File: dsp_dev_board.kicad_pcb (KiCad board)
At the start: 2 copper layers, 100 x 95 mm, 80 parts, among them J1 aux_mcu_power, J10 DX07S016JA1R1500, J11 I2Sext_SD, J12 I2S_SD, J13 SDOUT, J14 ~CSB, J15 I2S2_MCK, J16 WCLK, J17 BCLK, J18 SCLK, J2 audio_in, J3 audio_out, J4 9v_jack, J5 input_jack, J6 output_jack, J7 PD8-15 (digital), J8 PA0-7 (analog), J9 debug, U1 TL072, U2 AMS1117-3.3, U3 STM32F407VETx, U4 WM8731SEDS, Y1 8Mhz

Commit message: Progress
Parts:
- moved J13 115.3 mm to (211.4, 83.7)
- moved J15 105.5 mm to (205.7, 83.1)
- moved J16 96.5 mm to (200.3, 83.4)
- moved J17 86.2 mm to (194.6, 83.7)
- moved J18 85.7 mm to (178.5, 83.9)
- moved J14 75.8 mm to (183.3, 83.8)
- moved J12 69.9 mm to (174.2, 83.8)
- moved S1 68.8 mm to (148.7, 51.5)
- moved J9 66.0 mm to (195.2, 53.8)
- moved J11 65.8 mm to (188.5, 83.9)
- moved J1 63.9 mm to (166.1, 83.9)
- moved J7 55.3 mm to (211.2, 54.4), turned to 0 degrees
- moved D4 52.0 mm to (188.0, 46.7), turned to 270 degrees
- moved S2 49.0 mm to (141.6, 59.5), turned to 180 degrees
- moved D3 47.3 mm to (191.6, 46.7), turned to 90 degrees
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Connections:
- U1 pad 1: Net-(C4-Pad2) -> Net-(C5-Pad2)
- U1 pad 2: Net-(R5-Pad1) -> Net-(R6-Pad1)
- U1 pad 6: Net-(R6-Pad1) -> Net-(R5-Pad1)
- U1 pad 7: Net-(C5-Pad2) -> Net-(C4-Pad2)
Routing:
- net Net-(J7-Pad8): track 0.00 -> 61.0 mm, vias 0 -> 1
- net Net-(J7-Pad7): track 0.00 -> 59.7 mm, vias 0 -> 1
- net Net-(J7-Pad6): track 0.00 -> 58.9 mm, vias 0 -> 1
- net Net-(J7-Pad5): track 0.00 -> 58.2 mm, vias 0 -> 1
- net Net-(J7-Pad4): track 0.00 -> 57.4 mm, vias 0 -> 1
- net Net-(J7-Pad3): track 0.00 -> 56.6 mm, vias 0 -> 1
- net Net-(J7-Pad2): track 0.00 -> 56.2 mm, vias 0 -> 1
- net Net-(J7-Pad1): track 0.00 -> 54.8 mm, vias 0 -> 1
- net Net-(J8-Pad8): track 0.00 -> 45.0 mm, vias 0 -> 1
- net Net-(J8-Pad5): track 0.00 -> 44.2 mm, vias 0 -> 1
- net Net-(J8-Pad7): track 0.00 -> 44.0 mm, vias 0 -> 1
- net Net-(J8-Pad6): track 0.00 -> 43.9 mm, vias 0 -> 1
- net Net-(J8-Pad4): track 0.00 -> 43.0 mm, vias 0 -> 1
- net Net-(J8-Pad1): track 0.00 -> 41.8 mm, vias 0 -> 1
- net Net-(J8-Pad3): track 0.10 -> 40.2 mm, vias 0 -> 1
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- added copper zone on B.Cu, net 9V
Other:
- board text added: "Analog"
- board text added: "Boot"
- board text added: "PA0"
- board text added: "PA1"
- board text added: "PA2"
- board text added: "PA3"
- board text added: "PA4"
- board text added: "PA5"
- board text added: "PA6"
- board text added: "PA7"
- board text added: "Reset"

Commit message: USB to go
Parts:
- moved J9 63.6 mm to (131.7, 50.1)
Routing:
- net /MCU/OTG_FS_DM: track 0.00 -> 36.6 mm, vias 0 -> 2
- net VBUS: track 11.7 -> 46.6 mm, vias 0 -> 2
- net /MCU/OTG_FS_DP: track 0.00 -> 33.2 mm, vias 0 -> 2
- net 3.3V: track 111.1 -> 129.4 mm, vias 13 -> 17
- net GND: track 24.7 -> 35.5 mm
- net /MCU/NRST: track 20.0 -> 27.4 mm
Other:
- board size 100 x 95 mm -> 100 x 71.3 mm

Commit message: Lots of cleanup
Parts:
- moved J9 45.8 mm to (170.0, 75.3), turned to 270 degrees
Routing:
- net /MCU/SWCLK: track 0.00 -> 32.9 mm, vias 0 -> 3
- net /MCU/SWDIO: track 0.00 -> 27.8 mm, vias 0 -> 3
- net /MCU/TRACESWO: track 0.00 -> 27.4 mm, vias 0 -> 1
- net /audio_out: track 0.00 -> 25.5 mm, vias 0 -> 3
- net /audio_in: track 28.6 -> 49.2 mm, vias 2 -> 3
- net /MCU/NRST: track 27.4 -> 38.9 mm, vias 0 -> 1
- net VBUS: track 46.6 -> 54.4 mm, vias 2 -> 4
- net Net-(C4-Pad2): track 3.82 -> 10.7 mm, vias 0 -> 2
- net 3.3V: track 129.4 -> 124.0 mm

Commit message: Basically done?
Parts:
- removed J12: I2S_SD, Connector_PinHeader_2.54mm:PinHeader_1x02_P2.54mm_Vertical
- removed J13: SDOUT, Connector_PinHeader_2.54mm:PinHeader_1x02_P2.54mm_Vertical
- removed J14: ~CSB, Connector_PinHeader_2.54mm:PinHeader_1x02_P2.54mm_Vertical
- removed J15: I2S2_MCK, Connector_PinHeader_2.54mm:PinHeader_1x02_P2.54mm_Vertical
- removed J16: WCLK, Connector_PinHeader_2.54mm:PinHeader_1x02_P2.54mm_Vertical
- removed J17: BCLK, Connector_PinHeader_2.54mm:PinHeader_1x02_P2.54mm_Vertical
- removed J18: SCLK, Connector_PinHeader_2.54mm:PinHeader_1x02_P2.54mm_Vertical
- J11: value I2Sext_SD -> Conn_02x08_Odd_Even; footprint Connector_PinHeader_2.54mm:PinHeader_1x02_P2.54mm_Vertical -> Connector_PinHeader_2.54mm:PinHeader_2x08_P2.54mm_Vertical
- moved J1 53.2 mm to (124.9, 50.2), turned to 90 degrees
- moved J11 11.1 mm to (193.1, 73.8), turned to 270 degrees
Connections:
- J11 pad 1: /Codec/ADC -> /Codec/~CSB
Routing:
- net /audio_out: track 25.5 -> 70.1 mm, vias 3 -> 4
- net /Codec/~CSB: track 23.7 -> 38.2 mm, vias 1 -> 2
- net /Codec/SDIN: track 24.6 -> 37.5 mm, vias 1 -> 2
- net /Codec/WCLK: track 9.59 -> 21.8 mm
- net /Codec/BCLK: track 6.06 -> 17.9 mm, vias 1 -> 2
- net /Codec/ADC: track 5.84 -> 17.6 mm
- net /Codec/DAC: track 6.61 -> 18.0 mm
- net /Codec/SCLK: track 29.8 -> 39.6 mm, vias 1 -> 2
- net /MCU/I2S2_MCK: track 19.1 -> 28.7 mm, vias 1 -> 2
- net GND: track 35.5 -> 38.4 mm
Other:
- board text added: "DSP dev board v1 by Eric Wood and Matt Mullins"
- board text added: "aux power"

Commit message: it's done
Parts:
- added G***: LOGO, frankie:frankie, F.Cu at (131.2, 66.2)
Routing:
- net 3.3V: track 124.0 -> 130.6 mm, vias 17 -> 18
- net GND: track 38.4 -> 40.2 mm
- net /Codec/DAC: track 18.0 -> 19.3 mm
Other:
- board size 100 x 71.3 mm -> 100 x 60.3 mm
- board text added: "+3.3V"
- board text added: "BCLK"
- board text added: "DSP dev board v1 by Eric Wood"
- board text added: "Debug"
- board text added: "Digital"
- board text added: "GND"
- board text added: "I2S2_MCK"
- board text added: "I2S_SD"
- board text added: "I2Sext_SD"
- board text added: "PB4"
- board text added: "PB5"
- board text added: "PB6"
- board text added: "PB7"
- board text added: "PD10"
- board text added: "PD11"
- board text added: "PD12"
- board text added: "PD13"
- board text added: "PD14"
- board text added: "PD15"
- board text added: "PD8"
- board text added: "PD9"
- board text added: "SCLK"
- board text added: "SDOUT"
- board text added: "WCLK"
- board text added: "audio in"
- board text added: "gnd"
- board text added: "in"
- board text added: "input"
- board text added: "out"
- board text added: "output"
- board text added: "use this to play Frankie something nice"
- board text added: "~CSB"
- board text removed: "DSP dev board v1 by Eric Wood and Matt Mullins"
- board text removed: "aux power"

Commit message: 4 layer progress
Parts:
- removed G***: LOGO, frankie:frankie
- J10: footprint USB_C:JAE_DX07S016JA1R1500 -> DX07S016JA1R1500:JAE_DX07S016JA1R1500
- U4: moved to F.Cu
- moved C20 56.3 mm to (137.0, 95.3)
- moved C19 56.3 mm to (137.0, 93.7)
- moved J9 54.2 mm to (122.6, 101.7), turned to 90 degrees
- moved C18 53.6 mm to (123.5, 96.1)
- moved U2 50.1 mm to (118.8, 61.1), turned to 180 degrees
- moved D5 49.8 mm to (112.0, 69.5), turned to 0 degrees
- moved J2 49.4 mm to (171.5, 70.0)
- moved C1 48.7 mm to (124.8, 62.0), turned to 270 degrees
- moved C11 48.6 mm to (118.9, 82.0), turned to 90 degrees
- moved D6 48.3 mm to (112.0, 71.1), turned to 0 degrees
- moved D1 48.2 mm to (129.8, 63.0), turned to 0 degrees
- moved C17 48.0 mm to (116.6, 92.8)
- moved D7 47.0 mm to (112.0, 72.7), turned to 0 degrees
- moved C16 46.2 mm to (116.6, 89.7), turned to 90 degrees
- moved D8 45.9 mm to (112.0, 74.3), turned to 0 degrees
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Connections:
- R10 pad 1: /MCU/NRST -> 3.3V
- R10 pad 2: GND -> /MCU/NRST
- S2 pad C: 3.3V -> GND
- S2 pad D: 3.3V -> GND
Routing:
- net Net-(J7-Pad8): track 61.0 -> 0.00 mm, vias 1 -> 0
- net Net-(J7-Pad7): track 59.7 -> 0.00 mm, vias 1 -> 0
- net Net-(J7-Pad6): track 58.9 -> 0.00 mm, vias 1 -> 0
- net Net-(J7-Pad5): track 58.2 -> 0.00 mm, vias 1 -> 0
- net Net-(J7-Pad4): track 57.4 -> 0.00 mm, vias 1 -> 0
- net Net-(J7-Pad3): track 56.6 -> 0.00 mm, vias 1 -> 0
- net Net-(J7-Pad2): track 56.2 -> 0.00 mm, vias 1 -> 0
- net Net-(J7-Pad1): track 54.8 -> 0.00 mm, vias 1 -> 0
- net GND: track 40.2 -> 86.2 mm, vias 3 -> 17
- net 3.3V: track 130.6 -> 84.9 mm, vias 18 -> 4
- net Net-(J8-Pad8): track 45.0 -> 0.00 mm, vias 1 -> 0
- net Net-(J8-Pad5): track 44.2 -> 0.00 mm, vias 1 -> 0
- net Net-(J8-Pad7): track 44.0 -> 0.00 mm, vias 1 -> 0
- net Net-(J8-Pad6): track 43.9 -> 0.00 mm, vias 1 -> 0
- net Net-(J8-Pad4): track 43.0 -> 0.00 mm, vias 1 -> 0
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- added copper zone on F.Cu, net 3.3V
- added copper zone on In1.Cu, net GND
- added copper zone on In2.Cu, net GND
- removed copper zone on B.Cu, net 9V
- removed copper zone on F.Cu, net GND
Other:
- board size 100 x 60.3 mm -> 100 x 100 mm
- copper layers 2 -> 4
- board text removed: "+3.3V"
- board text removed: "Analog"
- board text removed: "BCLK"
- board text removed: "Boot"
- board text removed: "DSP dev board v1 by Eric Wood"
- board text removed: "Debug"
- board text removed: "Digital"
- board text removed: "GND"
- board text removed: "I2S2_MCK"
- board text removed: "I2S_SD"
- board text removed: "I2Sext_SD"
- board text removed: "PA0"
- board text removed: "PA1"
- board text removed: "PA2"
- board text removed: "PA3"
- board text removed: "PA4"
- board text removed: "PA5"
- board text removed: "PA6"
- board text removed: "PA7"
- board text removed: "PB4"
- board text removed: "PB5"
- board text removed: "PB6"
- board text removed: "PB7"
- board text removed: "PD10"
- board text removed: "PD11"
- board text removed: "PD12"
- board text removed: "PD13"
- board text removed: "PD14"
- board text removed: "PD15"
- board text removed: "PD8"
- board text removed: "PD9"
- board text removed: "Reset"
- board text removed: "SCLK"
- board text removed: "SDOUT"
- board text removed: "WCLK"
- board text removed: "audio in"
- board text removed: "gnd"
- board text removed: "in"
- board text removed: "input"
- board text removed: "out"
- board text removed: "output"
- board text removed: "use this to play Frankie something nice"
- board text removed: "~CSB"

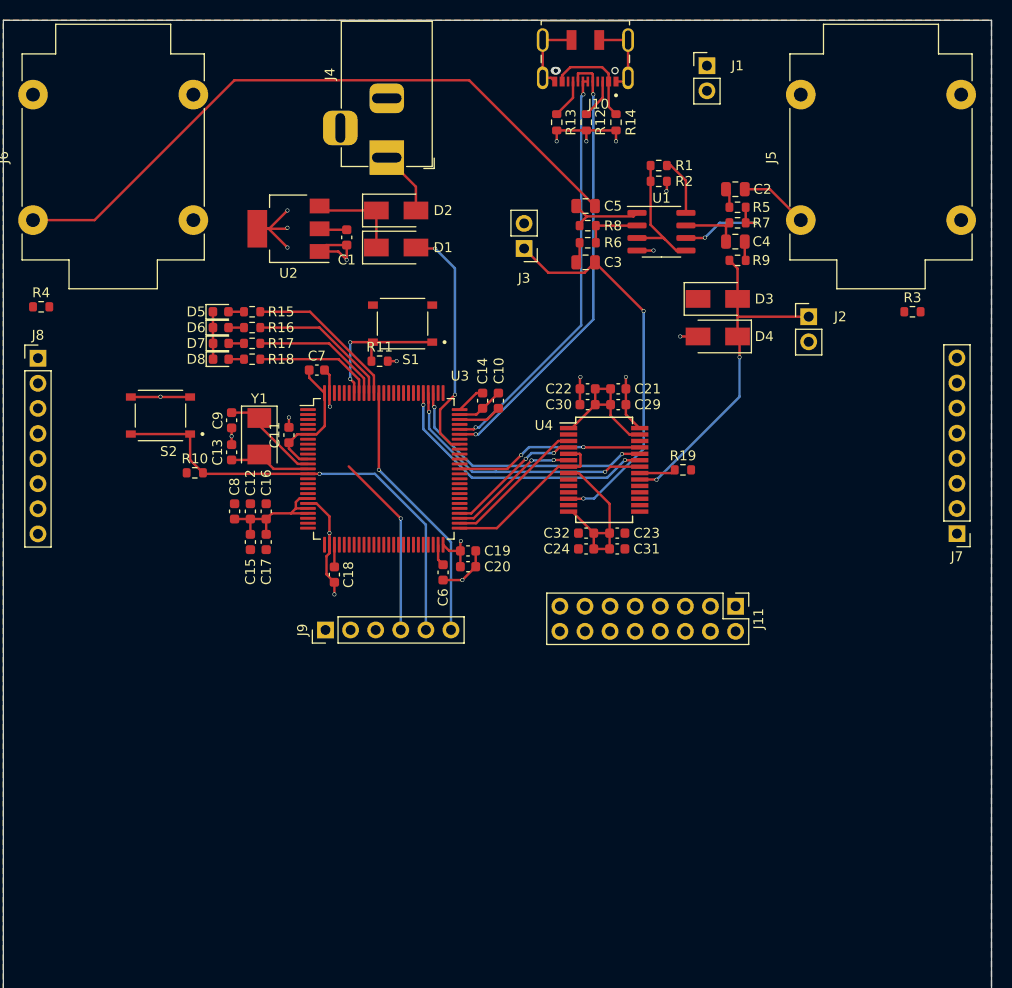
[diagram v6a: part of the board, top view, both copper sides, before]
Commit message: PCB: most major layout with both codec footprints
Surprisingly, I don't hate the really long I2S bus-like formation
between both footprints, though it does break up both the front and back
layers in the same orientation.
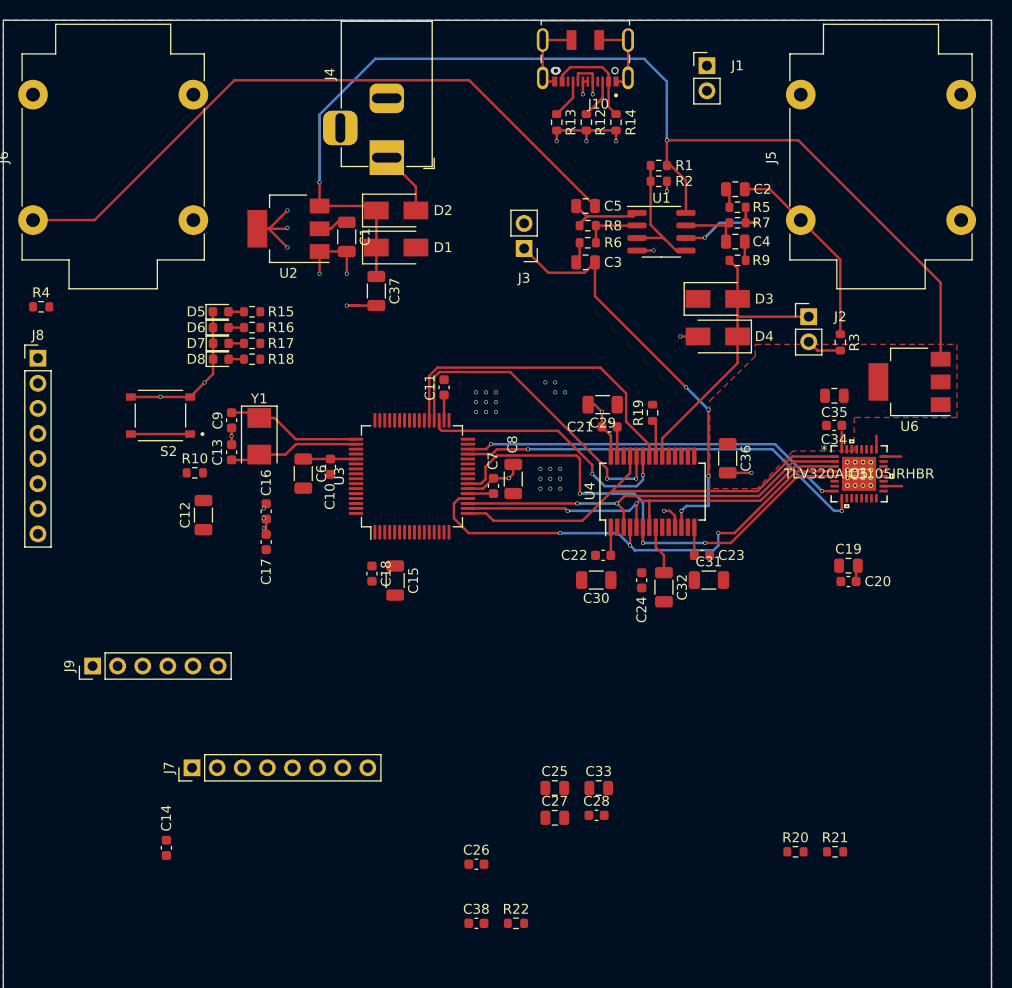
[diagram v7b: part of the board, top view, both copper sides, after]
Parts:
- removed J11: Conn_02x08_Odd_Even, Connector_PinHeader_2.54mm:PinHeader_2x08_P2.54mm_Vertical
- removed R11: 10k, Resistor_SMD:R_0603_1608Metric
- removed S1: TS-1187A-B-A-B, TactileSwitch:SW_TS-1187A-B-A-B
- added C25: 1u, Capacitor_SMD:C_0805_2012Metric, F.Cu at (145.8, 117.7)
- added C26: 100n, Capacitor_SMD:C_0603_1608Metric, F.Cu at (137.9, 125.4)
- added C27: 1u, Capacitor_SMD:C_0805_2012Metric, F.Cu at (145.8, 120.7)
- added C28: 100n, Capacitor_SMD:C_0603_1608Metric, F.Cu at (150.0, 120.5)
- added C33: 1u, Capacitor_SMD:C_0805_2012Metric, F.Cu at (150.2, 117.7)
- added C34: 100n, Capacitor_SMD:C_0603_1608Metric, F.Cu at (174.1, 81.0)
- added C35: 1u, Capacitor_SMD:C_0805_2012Metric, F.Cu at (174.1, 78.0)
- added C36: 10u, Capacitor_SMD:C_1206_3216Metric, F.Cu at (163.3, 84.3)
- added C37: 10u, Capacitor_SMD:C_1206_3216Metric, F.Cu at (127.8, 67.4)
- added C38: 100n, Capacitor_SMD:C_0603_1608Metric, F.Cu at (137.9, 131.4)
- added R20: 10k, Resistor_SMD:R_0603_1608Metric, F.Cu at (170.2, 124.2)
- added R21: 10k, Resistor_SMD:R_0603_1608Metric, F.Cu at (174.2, 124.2)
- added R22: 330, Resistor_SMD:R_0603_1608Metric, F.Cu at (141.9, 131.4)
- added U5: TLV320AIC3105IRHBR, TLV320AIC3105:TLV320AIC3105IRHBR, F.Cu at (176.6, 85.9)
- added U6: AMS1117-1.8, Package_TO_SOT_SMD:SOT-223-3_TabPin2, F.Cu at (181.7, 76.6)
- C1: value 0.1u -> 10u; footprint Capacitor_SMD:C_0603_1608Metric -> Capacitor_SMD:C_1206_3216Metric
- C10: value 2.2u -> 100n
- C12: value 100n -> 10u; footprint Capacitor_SMD:C_0603_1608Metric -> Capacitor_SMD:C_1206_3216Metric
- C15, C8: value 1u -> 10u; footprint Capacitor_SMD:C_0603_1608Metric -> Capacitor_SMD:C_1206_3216Metric
- C19: value 100n -> 1u; footprint Capacitor_SMD:C_0603_1608Metric -> Capacitor_SMD:C_0805_2012Metric
- C20: value 4.7u -> 100n
- C21, C22, C23, C24: value 0.1u -> 100n
- C29, C30, C31, C32: footprint Capacitor_SMD:C_0603_1608Metric -> Capacitor_SMD:C_1206_3216Metric
- C6: value 2.2u -> 10u; footprint Capacitor_SMD:C_0603_1608Metric -> Capacitor_SMD:C_1206_3216Metric
- J10: footprint DX07S016JA1R1500:JAE_DX07S016JA1R1500 -> USB_C:JAE_DX07S016JA1R1500
- J7: value PD8-15 (digital) -> digital
- J8: value PA0-7 (analog) -> analog
- U3: value STM32F407VETx -> ATSAME51J18A-A; footprint Package_QFP:LQFP-100_14x14mm_P0.5mm -> Package_QFP:TQFP-64_10x10mm_P0.5mm
- moved J7 80.9 mm to (109.1, 115.7), turned to 90 degrees
- moved C14 55.4 mm to (106.5, 123.8)
- moved C19 38.5 mm to (175.5, 95.2)
- moved C20 38.5 mm to (175.5, 96.8)
- moved C8 28.4 mm to (141.6, 86.4)
- moved J9 23.9 mm to (99.0, 105.3)
- moved C7 21.4 mm to (139.6, 87.1), turned to 90 degrees
- moved C10 18.3 mm to (123.1, 85.2), turned to 270 degrees
- moved C30 17.8 mm to (150.0, 96.7)
- moved C6 17.3 mm to (120.3, 85.9)
- moved C22 16.9 mm to (150.7, 94.2)
- moved C11 16.4 mm to (134.6, 77.2)
- moved C15 15.2 mm to (129.7, 96.7)
- moved C31 9.80 mm to (161.4, 96.7)
- moved C32 9.59 mm to (156.8, 97.4), turned to 270 degrees
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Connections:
- C10 pad 1: /MCU/VCAP_2 -> Net-(C10-Pad1)
- C17 pad 2: GND -> Net-(C17-Pad2)
- C19 pad 2: GND -> Net-(C17-Pad2)
- C20 pad 2: GND -> Net-(C17-Pad2)
- C6 pad 1: /MCU/VCAP_1 -> Net-(C10-Pad1)
- J7 pad 1: Net-(J7-Pad1) -> /MCU/PB00
- J7 pad 2: Net-(J7-Pad2) -> /MCU/PB01
- J7 pad 3: Net-(J7-Pad3) -> /MCU/PB02
- J7 pad 4: Net-(J7-Pad4) -> /MCU/PB03
- J7 pad 5: Net-(J7-Pad5) -> /MCU/PB04
- J7 pad 6: Net-(J7-Pad6) -> /MCU/PB05
- J7 pad 7: Net-(J7-Pad7) -> /MCU/PB06
- J7 pad 8: Net-(J7-Pad8) -> /MCU/PB07
- J8 pad 1: Net-(J8-Pad1) -> /MCU/PB08
- J8 pad 2: Net-(J8-Pad2) -> /MCU/PB09
- J8 pad 3: Net-(J8-Pad3) -> /MCU/PA02
- J8 pad 4: Net-(J8-Pad4) -> /MCU/PA03
- J8 pad 5: Net-(J8-Pad5) -> /MCU/PA04
- J8 pad 6: Net-(J8-Pad6) -> /MCU/PA05
- J8 pad 7: Net-(J8-Pad7) -> /MCU/PA06
- J8 pad 8: Net-(J8-Pad8) -> /MCU/PA07
- R10 pad 2: /MCU/NRST -> Net-(C38-Pad1)
- U3 pad 10: GND -> /MCU/PB07
- U3 pad 11: 3.3V -> /MCU/PB08
- U3 pad 12: /MCU/osc_in -> /MCU/PB09
- U3 pad 13: /MCU/osc_out -> /MCU/PA04
- U3 pad 14: /MCU/NRST -> /MCU/PA05
- U3 pad 15: Net-(U3-Pad15) -> /MCU/PA06
- U3 pad 16: Net-(U3-Pad16) -> /MCU/PA07
- U3 pad 17: Net-(U3-Pad17) -> /MCU/I2S2_MCK
- U3 pad 18: Net-(U3-Pad18) -> /Codec/WCLK
- U3 pad 19: 3.3V -> /Codec/BCLK
- U3 pad 20: GND -> /Codec/DAC
- U3 pad 22: 3.3V -> GND
- U3 pad 23: Net-(J8-Pad1) -> /Codec/ADC
- U3 pad 24: Net-(J8-Pad2) -> Net-(U3-Pad24)
- U3 pad 25: Net-(J8-Pad3) -> /MCU/led1
- U3 pad 26: Net-(J8-Pad4) -> /MCU/led2
- U3 pad 27: GND -> /MCU/led3
- U3 pad 28: 3.3V -> /MCU/led4
- U3 pad 29: Net-(J8-Pad5) -> /MCU/SDA
- U3 pad 3: Net-(U3-Pad3) -> /MCU/PA02
- U3 pad 30: Net-(J8-Pad6) -> /MCU/SCL
- U3 pad 31: Net-(J8-Pad7) -> /MCU/~CODEC_RST
- U3 pad 32: Net-(J8-Pad8) -> /MCU/BOOT0
- U3 pad 33: Net-(U3-Pad33) -> GND
- U3 pad 34: Net-(U3-Pad34) -> 3.3V
- U3 pad 35: Net-(U3-Pad35) -> /Codec/SDIN
- U3 pad 36: Net-(U3-Pad36) -> /Codec/SCLK
- U3 pad 37: Net-(U3-Pad37) -> /Codec/~CSB
- U3 pad 4: Net-(U3-Pad4) -> /MCU/PA03
- U3 pad 45: Net-(U3-Pad45) -> /MCU/OTG_FS_DM
- U3 pad 46: Net-(U3-Pad46) -> /MCU/OTG_FS_DP
- U3 pad 47: Net-(U3-Pad47) -> GND
- U3 pad 48: Net-(U3-Pad48) -> 3.3V
- U3 pad 49: /MCU/VCAP_1 -> /MCU/osc_in
- U3 pad 5: Net-(U3-Pad5) -> /MCU/PB04
- U3 pad 50: 3.3V -> /MCU/osc_out
- U3 pad 51: /Codec/WCLK -> Net-(U3-Pad51)
- U3 pad 52: /Codec/BCLK -> Net-(C38-Pad1)
- U3 pad 53: /Codec/ADC -> Net-(C10-Pad1)
- U3 pad 54: /Codec/DAC -> GND
- U3 pad 55: Net-(J7-Pad1) -> Net-(U3-Pad55)
- U3 pad 56: Net-(J7-Pad2) -> 3.3V
- U3 pad 57: Net-(J7-Pad3) -> /MCU/SWCLK
- U3 pad 58: Net-(J7-Pad4) -> /MCU/SWDIO
- U3 pad 59: Net-(J7-Pad5) -> /MCU/TRACESWO
- U3 pad 6: 3.3V -> /MCU/PB05
- U3 pad 60: Net-(J7-Pad6) -> Net-(U3-Pad60)
- U3 pad 61: Net-(J7-Pad7) -> /MCU/PB00
- U3 pad 62: Net-(J7-Pad8) -> /MCU/PB01
- U3 pad 63: /MCU/I2S2_MCK -> /MCU/PB02
- U3 pad 64: Net-(U3-Pad64) -> /MCU/PB03
- U3 pad 7: Net-(U3-Pad7) -> GND
- U3 pad 8: Net-(U3-Pad8) -> 3.3V
- U3 pad 9: Net-(U3-Pad9) -> /MCU/PB06
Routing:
- net 9V: track 15.5 -> 116.8 mm, vias 0 -> 2
- net 3.3V: track 84.9 -> 39.0 mm, vias 4 -> 28
- net /MCU/SDA: track 0.00 -> 41.9 mm, vias 0 -> 2
- net /MCU/OTG_FS_DM: track 45.5 -> 4.39 mm, vias 2 -> 1
- net /MCU/OTG_FS_DP: track 41.9 -> 1.82 mm, vias 2 -> 1
- net /MCU/NRST: track 45.8 -> 6.00 mm, vias 1 -> 0
- net /MCU/SCL: track 0.00 -> 39.3 mm, vias 0 -> 2
- net /Codec/ADC: track 13.5 -> 51.6 mm, vias 2 -> 3
- net /Codec/DAC: track 13.8 -> 48.9 mm, vias 2 -> 3
- net /Codec/BCLK: track 14.5 -> 41.6 mm, vias 0 -> 2
- net /MCU/TRACESWO: track 27.0 -> 0.00 mm, vias 1 -> 0
- net /Codec/WCLK: track 17.2 -> 44.2 mm, vias 0 -> 2
- net /MCU/I2S2_MCK: track 19.1 -> 44.4 mm, vias 2 -> 0
- net VBUS: track 34.9 -> 10.5 mm, vias 2 -> 0
- net /MCU/SWDIO: track 18.7 -> 0.00 mm, vias 1 -> 0
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- added copper zone on F.Cu, net 1.8V
